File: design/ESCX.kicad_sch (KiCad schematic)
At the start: 22 parts, among them J1 HALL_ENC, J2 COMM, J3 SERVO, J4 SWD, J5 USB_OTG, SW1 SENSOR_VOLTAGE

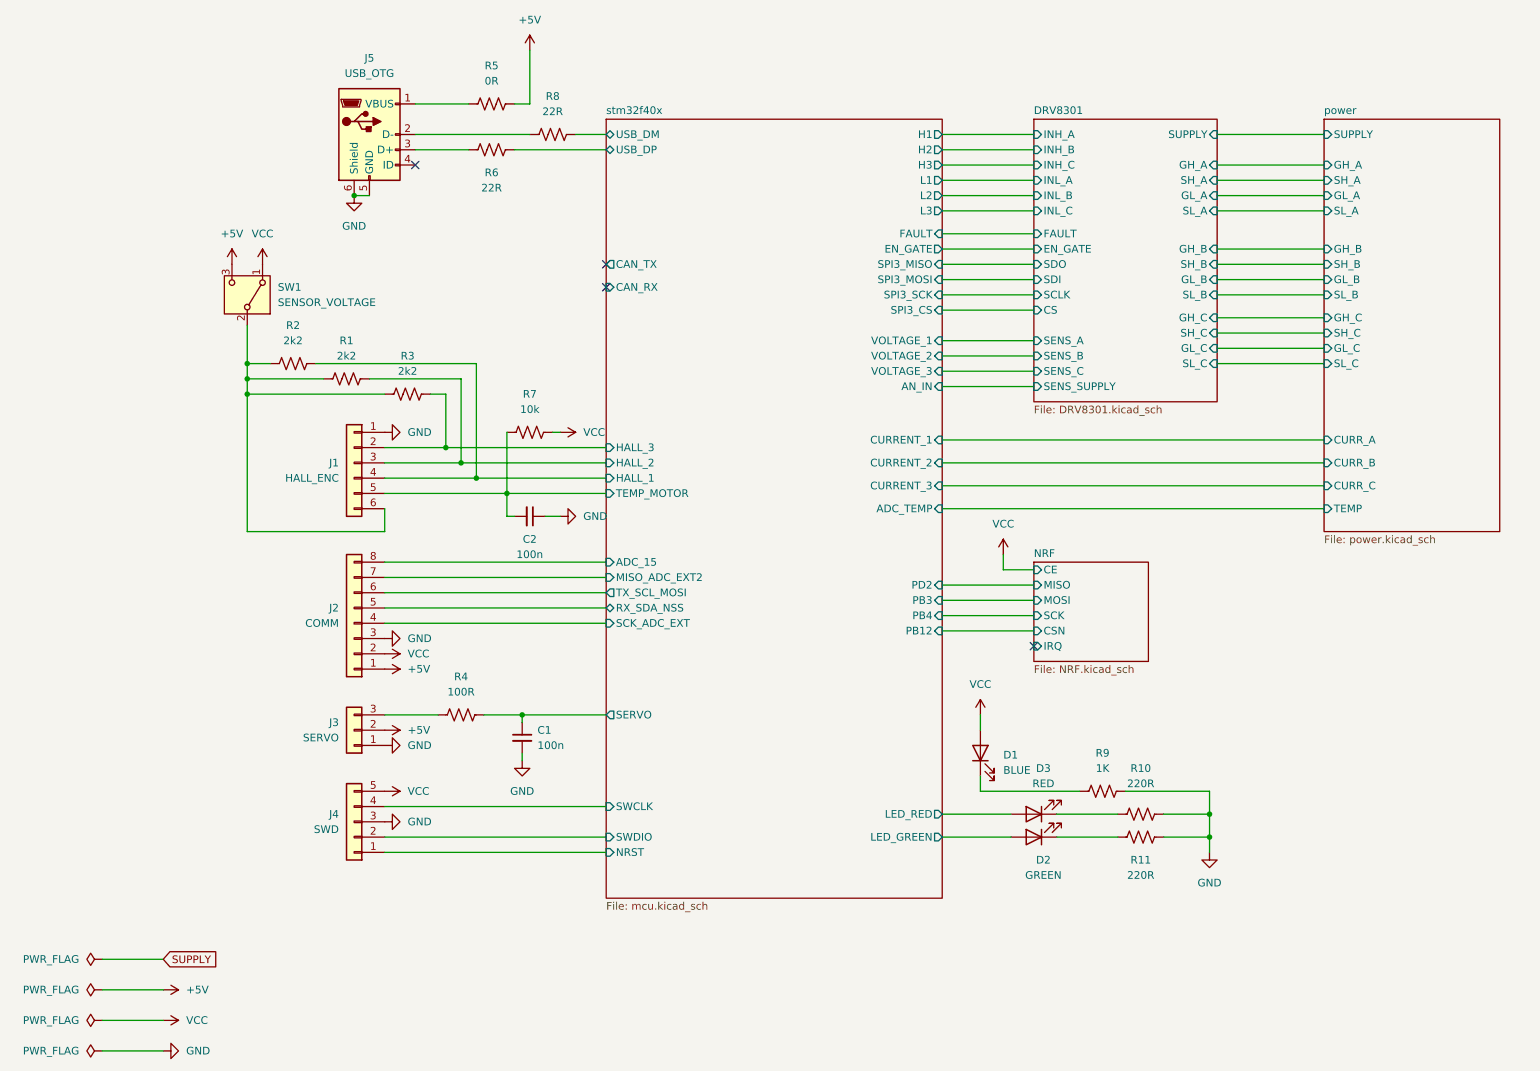
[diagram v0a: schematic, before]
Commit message: Impresión de esquemático en pdf
Impresión de la versión del esquemático en la carpeta /pdf
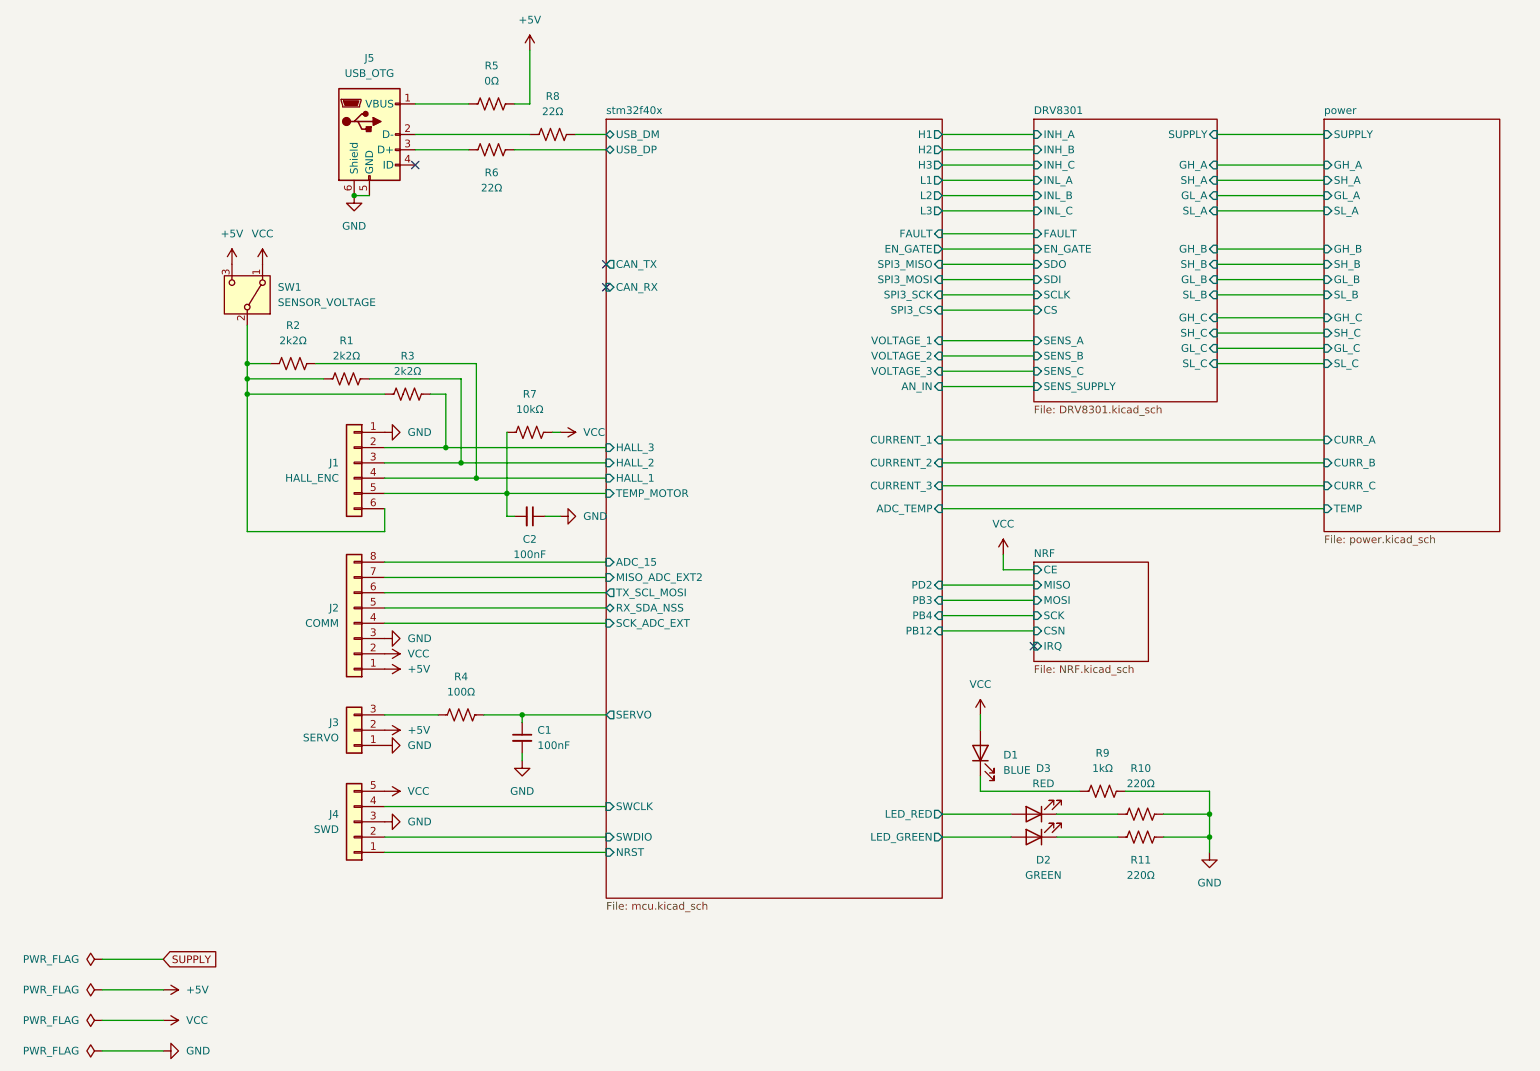
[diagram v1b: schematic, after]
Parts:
- C1, C2: value 100n -> 100nF
- R1, R2, R3: value 2k2 -> 2k2Ω
- R10, R11: value 220R -> 220Ω
- R4: value 100R -> 100Ω
- R5: value 0R -> 0Ω
- R6, R8: value 22R -> 22Ω
- R7: value 10k -> 10kΩ
- R9: value 1K -> 1kΩ
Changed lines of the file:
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@@
 			)
 		)
-		(property "Value" "2k2"
+		(property "Value" "2k2Ω"
 			(at 83.82 74.93 90)
 			(effects
@@
 			)
 		)
-		(property "Value" "2k2"
+		(property "Value" "2k2Ω"
 			(at 73.66 72.39 90)
 			(effects
@@
 			)
 		)
-		(property "Value" "2k2"
+		(property "Value" "2k2Ω"
 			(at 64.77 69.85 90)
 			(effects
@@
 			)
 		)
-		(property "Value" "10k"
+		(property "Value" "10kΩ"
 			(at 104.14 81.28 90)
 			(effects
@@
 			)
 		)
-		(property "Value" "100n"
+		(property "Value" "100nF"
 			(at 104.1336 105.41 90)
 			(effects
@@
 			)
 		)
-		(property "Value" "22R"
+		(property "Value" "22Ω"
 			(at 107.95 31.75 90)
 			(effects
@@
 			)
 		)
-		(property "Value" "22R"
+		(property "Value" "22Ω"
 			(at 97.79 44.45 90)
 			(effects
@@
 			)
 		)
-		(property "Value" "100R"
+		(property "Value" "100Ω"
 			(at 92.71 128.27 90)
 			(effects
@@
 			)
 		)
-		(property "Value" "100n"
+		(property "Value" "100nF"
 			(at 105.41 137.1662 0)
 			(effects
@@
 			)
 		)
-		(property "Value" "1K"
+		(property "Value" "1kΩ"
 			(at 199.39 140.97 90)
 			(effects
@@
 			)
 		)
-		(property "Value" "220R"
+		(property "Value" "220Ω"
 			(at 205.74 143.51 90)
 			(effects
@@
 			)
 		)
-		(property "Value" "220R"
+		(property "Value" "220Ω"
 			(at 205.74 158.75 90)
 			(effects
@@
 			)
 		)
-		(property "Value" "0R"
+		(property "Value" "0Ω"
 			(at 97.79 26.67 90)
 			(effects
@@
 			)
 		)
-		(property "Description" "R 0, 0603 "
+		(property "Description" "RES 0 OHM 1% 1/10W 0603"
 			(at 97.79 30.48 0)
 			(effects

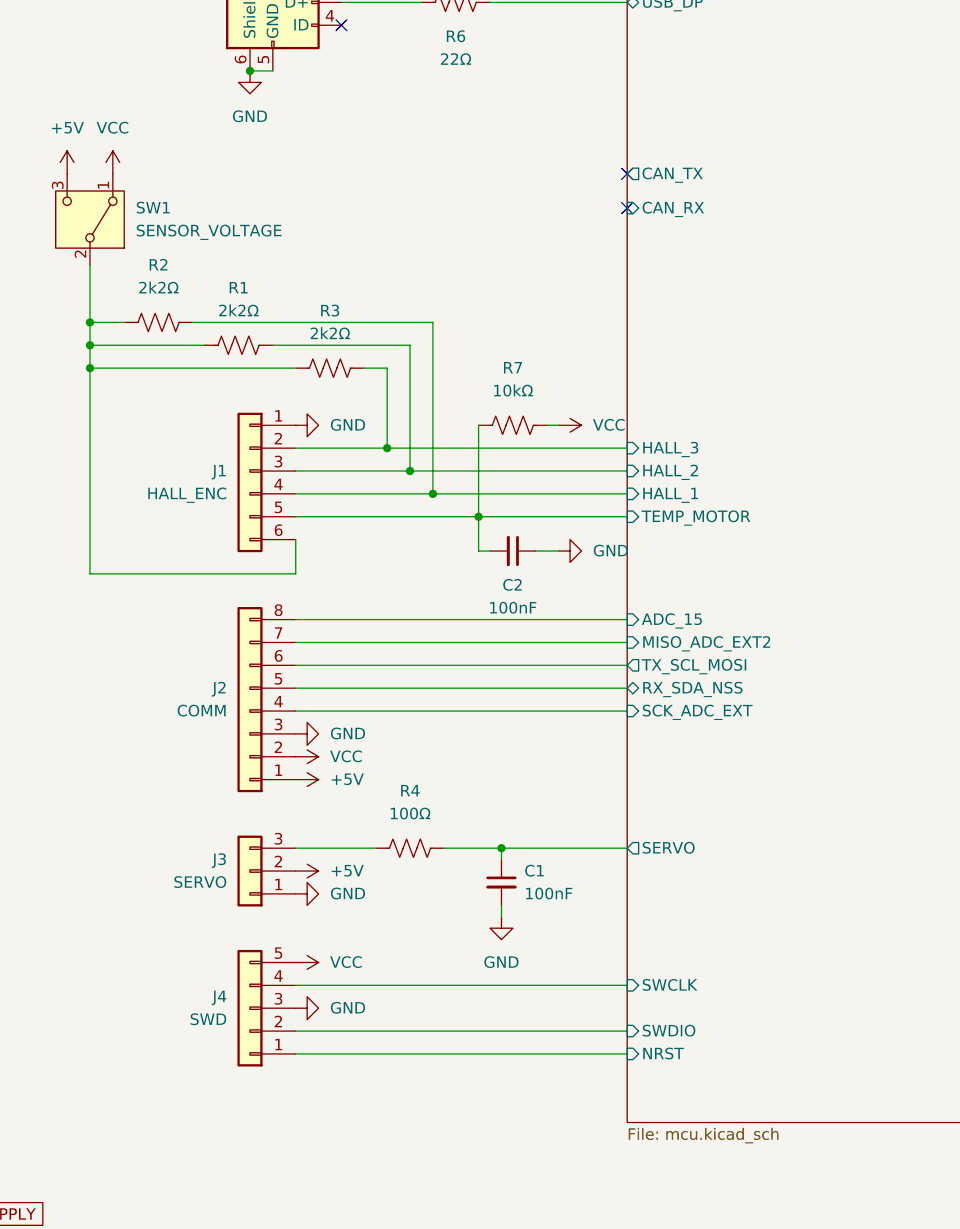
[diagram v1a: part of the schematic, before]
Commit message: Pequeños cambios
Se sacaron y se marcaron como NC:
	* CAN_TX y CAN_RX (no se usa CAN).
	* SERVO (no vamos a manejar servomotores).
	* ADC_15, MISO_ADC_EXT, TX_SCL_MOSI, RX_SDA_NSS, SCK_ADC_EXT (sin ADC externo ni acelerómetro).
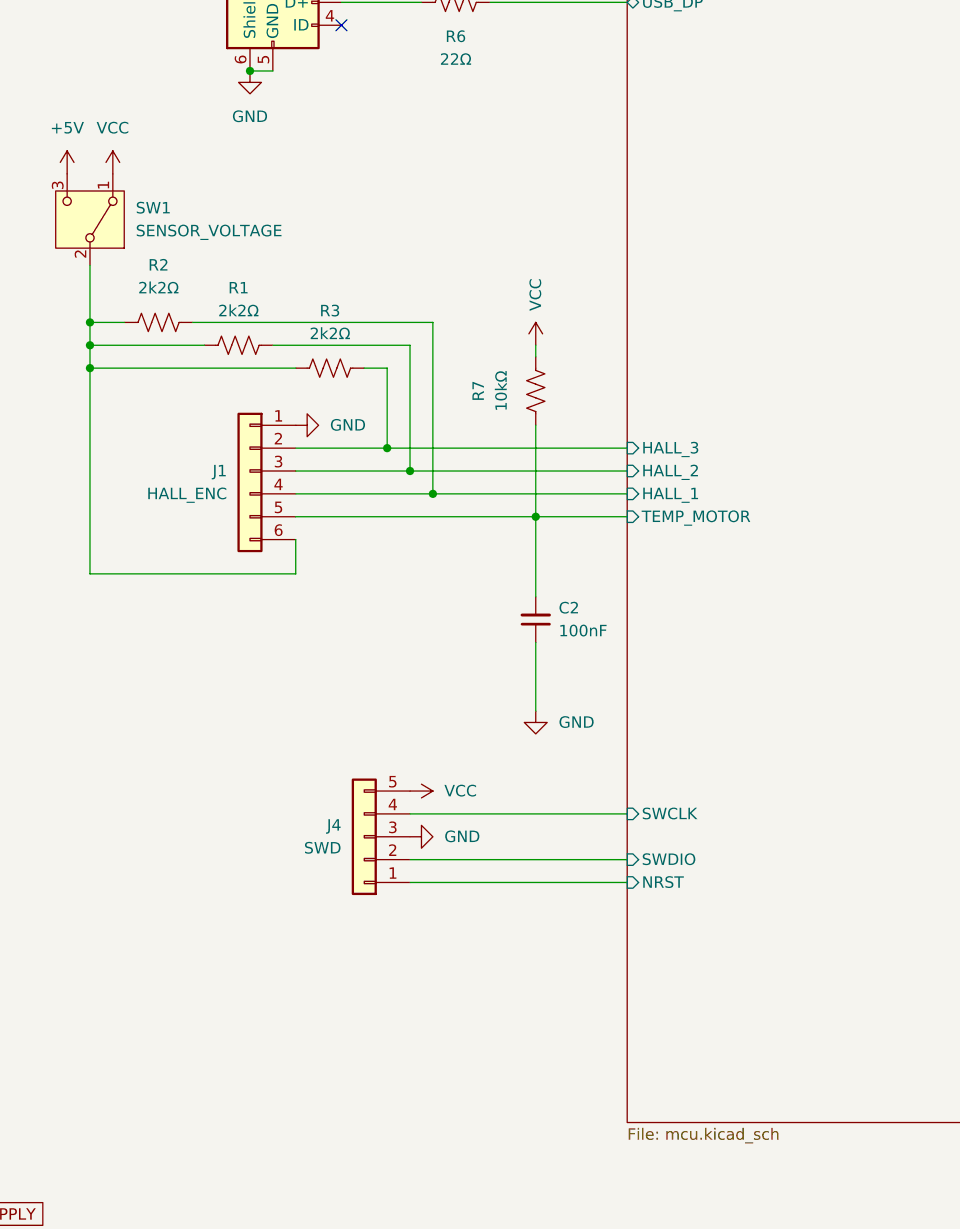
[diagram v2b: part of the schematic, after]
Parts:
- removed C1: 100nF, Capacitor_SMD:C_0603_1608Metric, symbol Device:C_Small
- removed J2: COMM, symbol Connector_Generic:Conn_01x08
- removed J3: SERVO, symbol Connector_Generic:Conn_01x03
- removed R4: 100Ω, Resistor_SMD:R_0603_1608Metric, symbol Device:R_US
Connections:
- no-connect marks 4 -> 2
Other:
- sheet stm32f40x ports: added none; removed ADC_15, CAN_RX, CAN_TX, MISO_ADC_EXT2, RX_SDA_NSS, SCK_ADC_EXT, SERVO, TX_SCL_MOSI
- moved on the sheet: C2, J4, R7

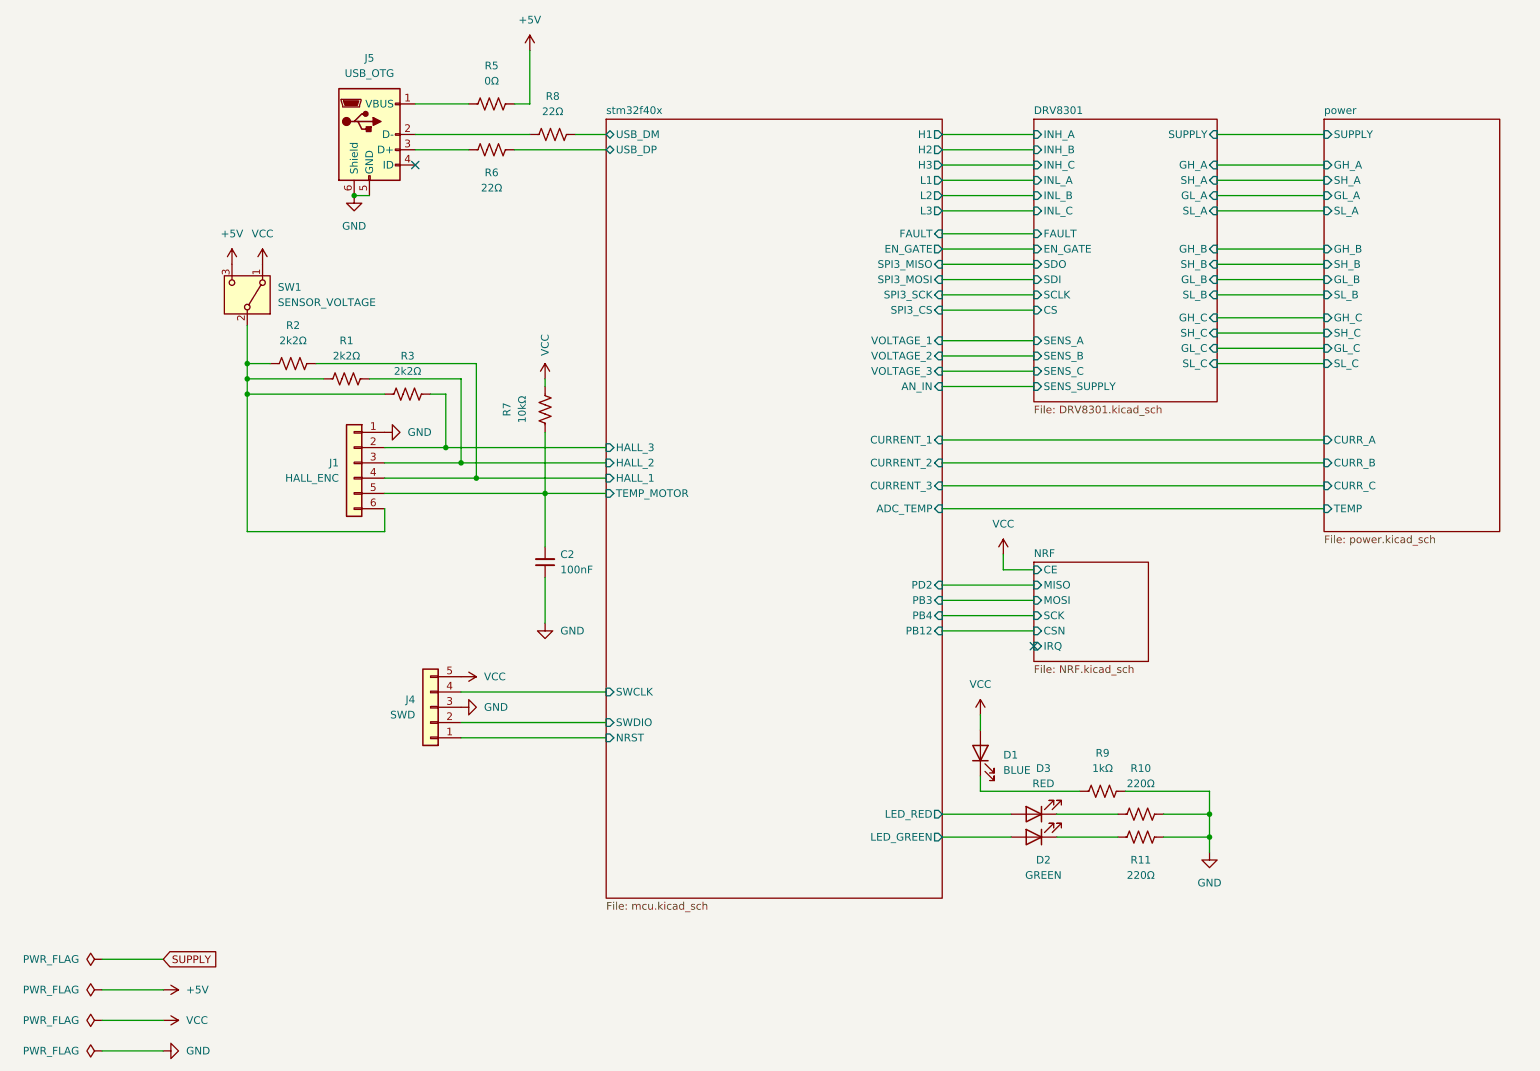
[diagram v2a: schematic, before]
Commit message: Agregado ibom
Pequeños cambios en el esquemático y agregado de ibom
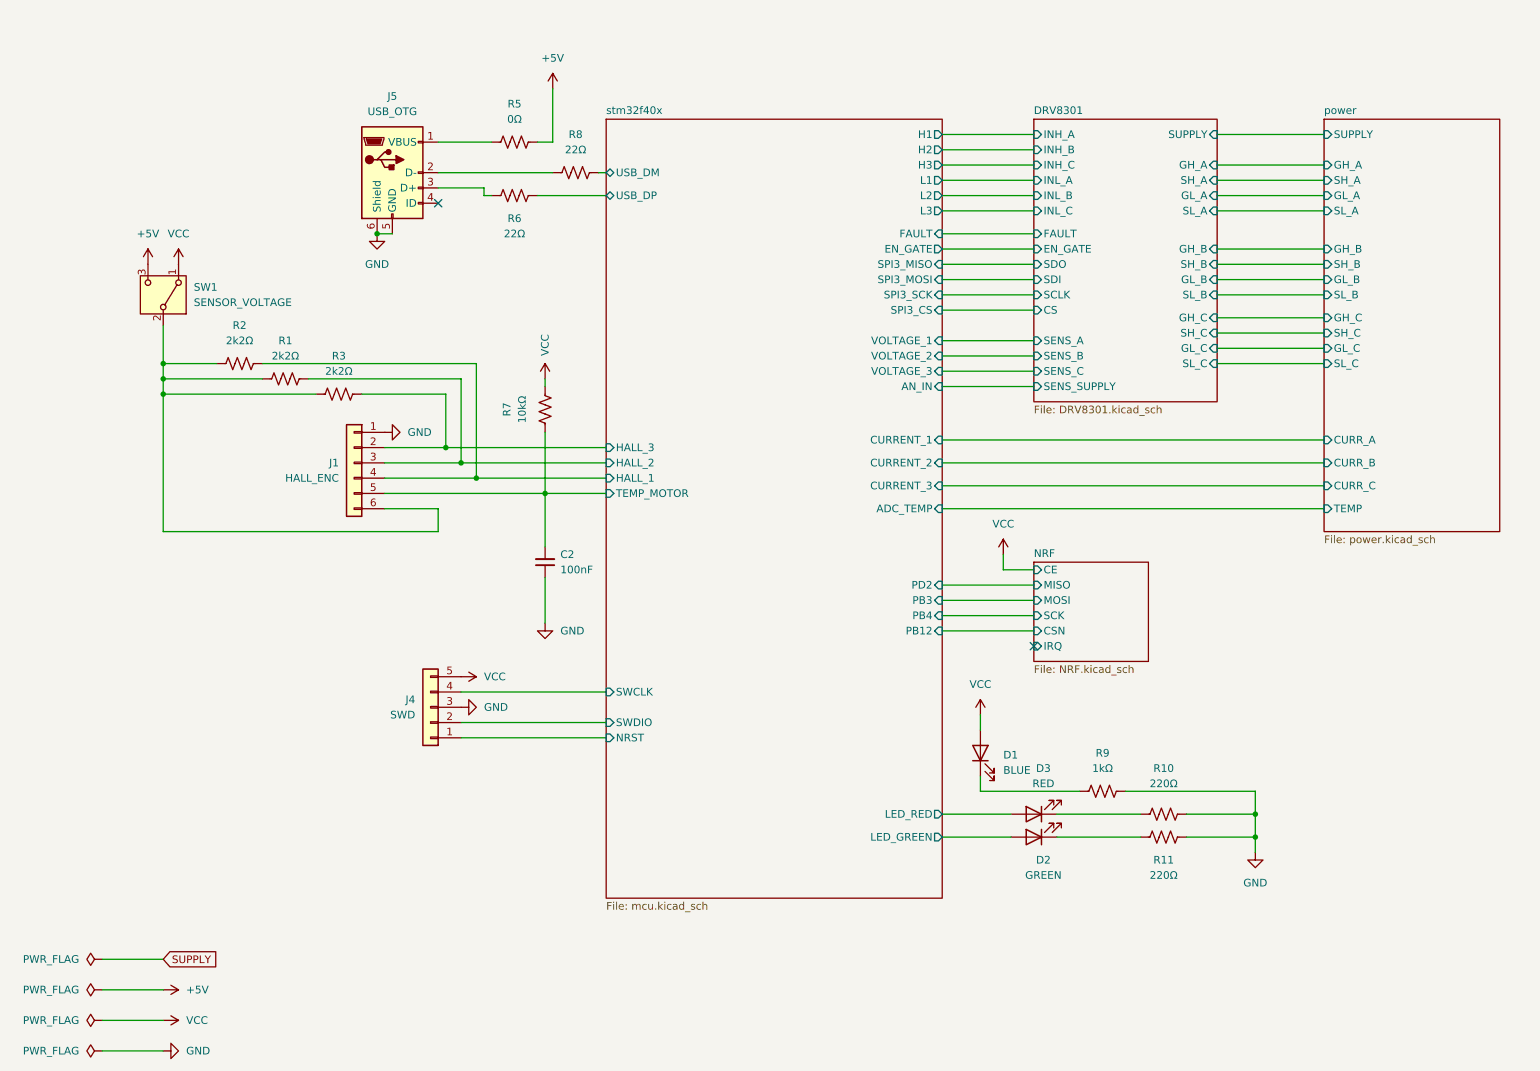
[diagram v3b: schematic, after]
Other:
- moved on the sheet: J5, R1, R10, R11, R2, R3, R5, R6, R8, SW1
